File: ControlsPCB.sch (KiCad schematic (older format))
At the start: 7 parts, among them J1 8P8C_Shielded, J2 8P8C_Shielded

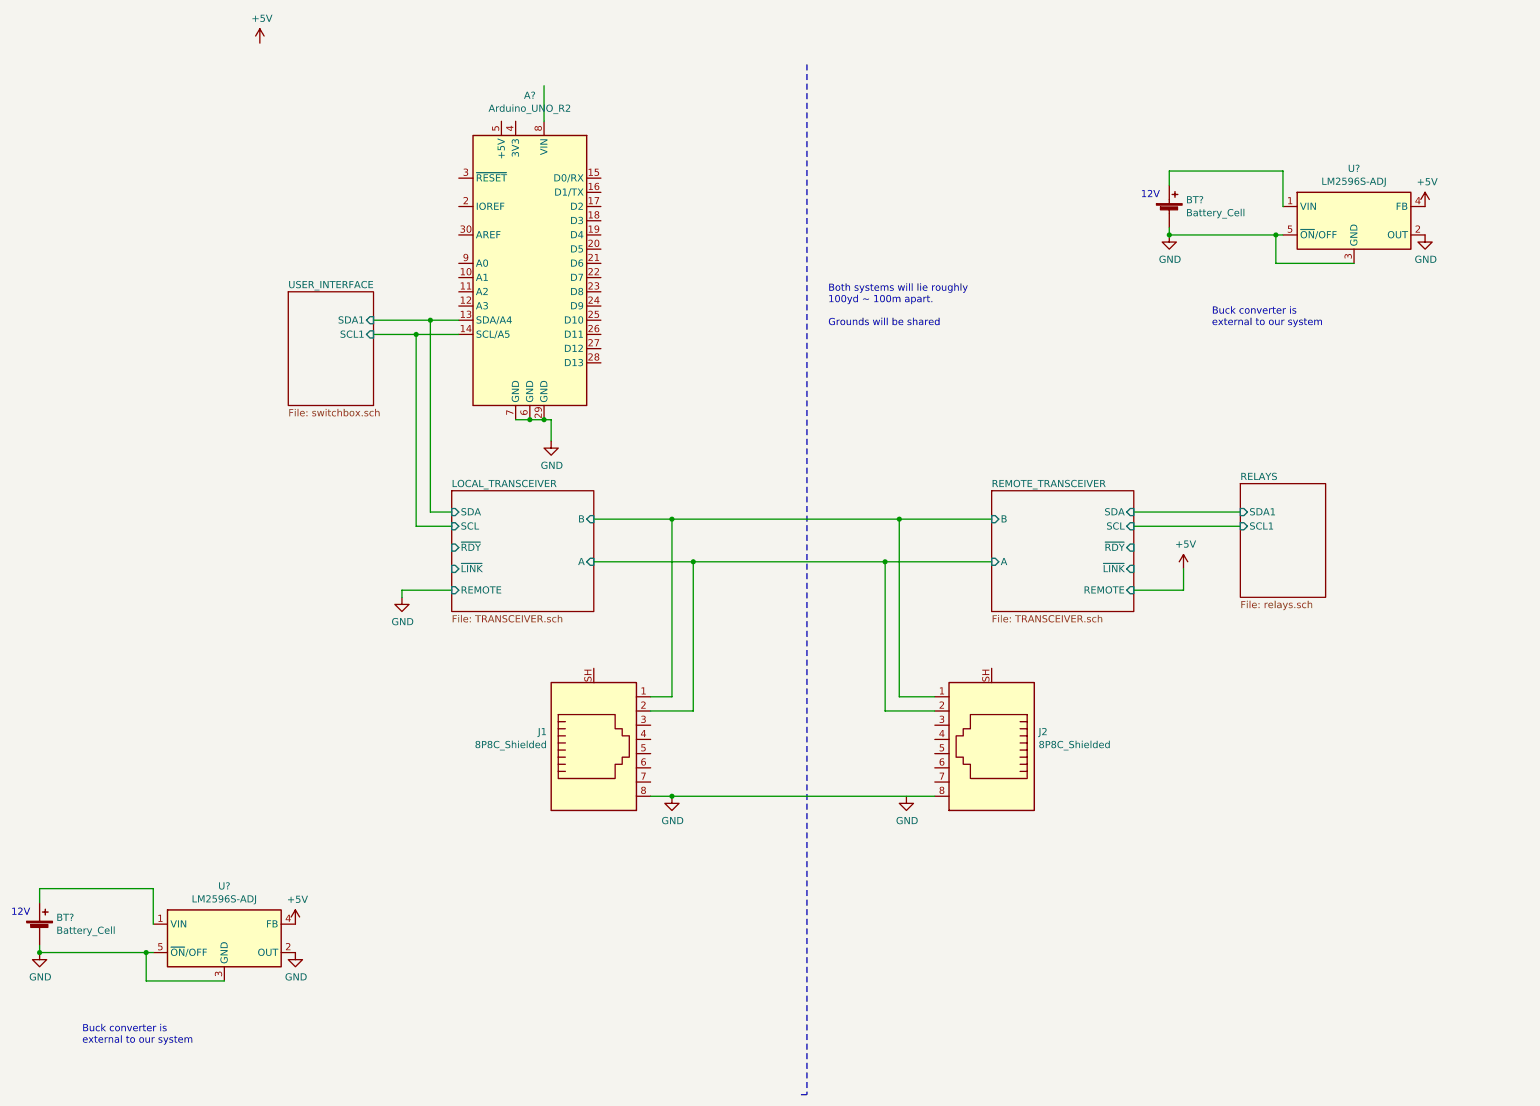
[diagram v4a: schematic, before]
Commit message: Got rid of overlying duplicate parts
Some identical parts were placed over eachother which showed up when annotating references
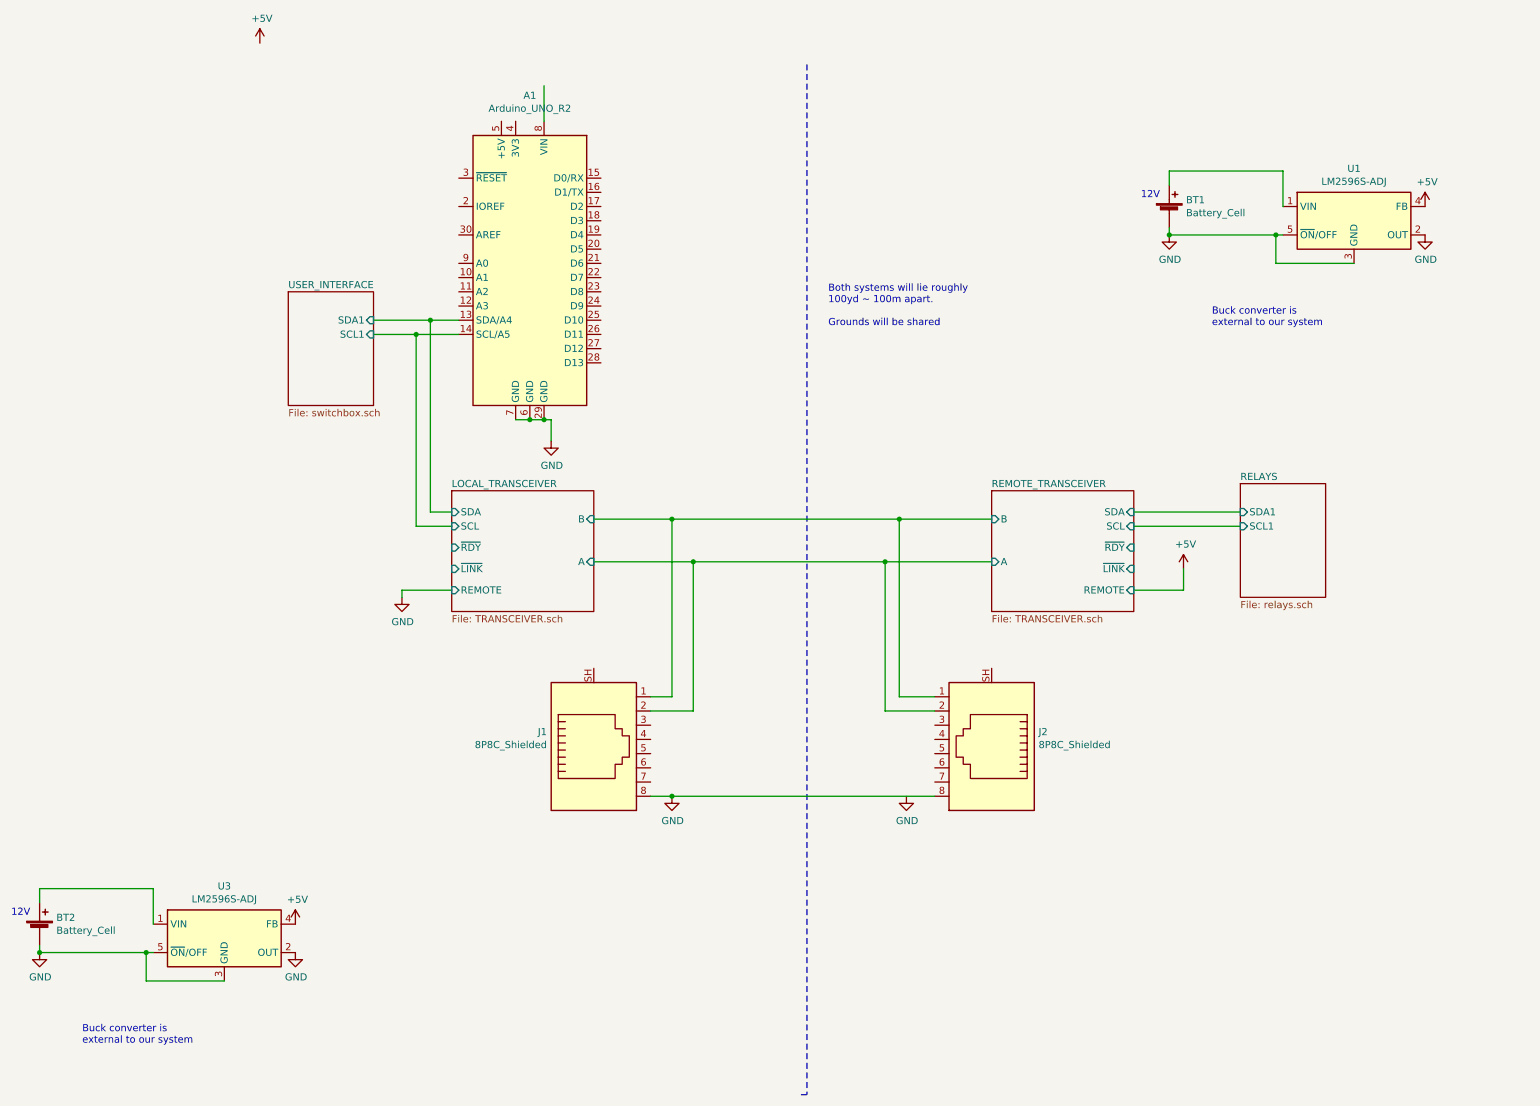
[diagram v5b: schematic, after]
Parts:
- gave numbers to parts that had none: 5
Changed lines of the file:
@@
 P 2650 6600
 AR Path="/5F57B52C/5F73A08B" Ref="#PWR?"  Part="1"
-AR Path="/5F73A08B" Ref="#PWR?"  Part="1"
-F 0 "#PWR?" H 2650 6450 50  0001 C CNN
+AR Path="/5F73A08B" Ref="#PWR0114"  Part="1"
+F 0 "#PWR0114" H 2650 6450 50  0001 C CNN
 F 1 "+5V" H 2665 6773 50  0000 C CNN
 F 2 "" H 2650 6600 50  0001 C CNN
@@
 P 2650 6800
 AR Path="/5F57B52C/5F73A091" Ref="#PWR?"  Part="1"
-AR Path="/5F73A091" Ref="#PWR?"  Part="1"
-F 0 "#PWR?" H 2650 6550 50  0001 C CNN
+AR Path="/5F73A091" Ref="#PWR0115"  Part="1"
+F 0 "#PWR0115" H 2650 6550 50  0001 C CNN
 F 1 "GND" H 2655 6627 50  0000 C CNN
 F 2 "" H 2650 6800 50  0001 C CNN
@@
 P 2150 6700
 AR Path="/5F57B52C/5F73A0A3" Ref="U?"  Part="1"
-AR Path="/5F73A0A3" Ref="U?"  Part="1"
-F 0 "U?" H 2150 7067 50  0000 C CNN
+AR Path="/5F73A0A3" Ref="U3"  Part="1"
+F 0 "U3" H 2150 7067 50  0000 C CNN
 F 1 "LM2596S-ADJ" H 2150 6976 50  0000 C CNN
 F 2 "Package_TO_SOT_SMD:TO-263-5_TabPin3" H 2200 6450 50  0001 L CIN
@@
 P 850 6650
 AR Path="/5F57B52C/5F73A0A9" Ref="BT?"  Part="1"
-AR Path="/5F73A0A9" Ref="BT?"  Part="1"
-F 0 "BT?" H 968 6746 50  0000 L CNN
+AR Path="/5F73A0A9" Ref="BT2"  Part="1"
+F 0 "BT2" H 968 6746 50  0000 L CNN
 F 1 "Battery_Cell" H 968 6655 50  0000 L CNN
 F 2 "" V 850 6710 50  0001 C CNN
@@
 P 850 6800
 AR Path="/5F57B52C/5F73EC1F" Ref="#PWR?"  Part="1"
-AR Path="/5F73EC1F" Ref="#PWR?"  Part="1"
-F 0 "#PWR?" H 850 6550 50  0001 C CNN
+AR Path="/5F73EC1F" Ref="#PWR0125"  Part="1"
+F 0 "#PWR0125" H 850 6550 50  0001 C CNN
 F 1 "GND" H 855 6627 50  0000 C CNN
 F 2 "" H 850 6800 50  0001 C CNN
@@
 Connection ~ 850  6800
 $Comp
-L MCU_Module:Arduino_UNO_R2 A?
+L MCU_Module:Arduino_UNO_R2 A1
 U 1 1 5F74B67E
 P 4300 1950
-AR Path="/5F74B67E" Ref="A?"  Part="1"
+AR Path="/5F74B67E" Ref="A1"  Part="1"
 AR Path="/5F6BFC31/5F74B67E" Ref="A?"  Part="1"
-F 0 "A?" H 4300 3131 50  0000 C CNN
+F 0 "A1" H 4300 3131 50  0000 C CNN
 F 1 "Arduino_UNO_R2" H 4300 3040 50  0000 C CNN
 F 2 "Module:Arduino_UNO_R2" H 4300 1950 50  0001 C CIN
@@
 P 2400 400
 AR Path="/5F57B52C/5F7512D5" Ref="#PWR?"  Part="1"
-AR Path="/5F7512D5" Ref="#PWR?"  Part="1"
-F 0 "#PWR?" H 2400 250 50  0001 C CNN
+AR Path="/5F7512D5" Ref="#PWR0126"  Part="1"
+F 0 "#PWR0126" H 2400 250 50  0001 C CNN
 F 1 "+5V" H 2415 573 50  0000 C CNN
 F 2 "" H 2400 400 50  0001 C CNN
@@
 	4400 3050 4450 3050
 $Comp
-L power:GND #PWR?
+L power:GND #PWR0127
 U 1 1 5F753983
 P 4450 3200
-F 0 "#PWR?" H 4450 2950 50  0001 C CNN
+F 0 "#PWR0127" H 4450 2950 50  0001 C CNN
 F 1 "GND" H 4455 3027 50  0000 C CNN
 F 2 "" H 4450 3200 50  0001 C CNN
@@
 	3500 2450 3800 2450
 $Comp
-L power:GND #PWR?
+L power:GND #PWR0128
 U 1 1 5F78DE7A
 P 3400 4300
-F 0 "#PWR?" H 3400 4050 50  0001 C CNN
+F 0 "#PWR0128" H 3400 4050 50  0001 C CNN
 F 1 "GND" H 3405 4127 50  0000 C CNN
 F 2 "" H 3400 4300 50  0001 C CNN
@@
 	3400 4250 3750 4250
 $Comp
-L power:+5V #PWR?
+L power:+5V #PWR0129
 U 1 1 5F7956F2
 P 8900 4100
-F 0 "#PWR?" H 8900 3950 50  0001 C CNN
+F 0 "#PWR0129" H 8900 3950 50  0001 C CNN
 F 1 "+5V" H 8915 4273 50  0000 C CNN
 F 2 "" H 8900 4100 50  0001 C CNN
@@
 P 10600 1550
 AR Path="/5F57B52C/5F7F4E76" Ref="#PWR?"  Part="1"
-AR Path="/5F7F4E76" Ref="#PWR?"  Part="1"
-F 0 "#PWR?" H 10600 1400 50  0001 C CNN
+AR Path="/5F7F4E76" Ref="#PWR0130"  Part="1"
+F 0 "#PWR0130" H 10600 1400 50  0001 C CNN
 F 1 "+5V" H 10615 1723 50  0000 C CNN
 F 2 "" H 10600 1550 50  0001 C CNN
@@
 P 10600 1750
 AR Path="/5F57B52C/5F7F4E7C" Ref="#PWR?"  Part="1"
-AR Path="/5F7F4E7C" Ref="#PWR?"  Part="1"
-F 0 "#PWR?" H 10600 1500 50  0001 C CNN
+AR Path="/5F7F4E7C" Ref="#PWR0131"  Part="1"
+F 0 "#PWR0131" H 10600 1500 50  0001 C CNN
 F 1 "GND" H 10605 1577 50  0000 C CNN
 F 2 "" H 10600 1750 50  0001 C CNN
@@
 P 10100 1650
 AR Path="/5F57B52C/5F7F4E83" Ref="U?"  Part="1"
-AR Path="/5F7F4E83" Ref="U?"  Part="1"
-F 0 "U?" H 10100 2017 50  0000 C CNN
+AR Path="/5F7F4E83" Ref="U1"  Part="1"
+F 0 "U1" H 10100 2017 50  0000 C CNN
 F 1 "LM2596S-ADJ" H 10100 1926 50  0000 C CNN
 F 2 "Package_TO_SOT_SMD:TO-263-5_TabPin3" H 10150 1400 50  0001 L CIN
@@
 P 8800 1600
 AR Path="/5F57B52C/5F7F4E89" Ref="BT?"  Part="1"
-AR Path="/5F7F4E89" Ref="BT?"  Part="1"
-F 0 "BT?" H 8918 1696 50  0000 L CNN
+AR Path="/5F7F4E89" Ref="BT1"  Part="1"
+F 0 "BT1" H 8918 1696 50  0000 L CNN
 F 1 "Battery_Cell" H 8918 1605 50  0000 L CNN
 F 2 "" V 8800 1660 50  0001 C CNN
@@
 P 8800 1750
 AR Path="/5F57B52C/5F7F4E99" Ref="#PWR?"  Part="1"
-AR Path="/5F7F4E99" Ref="#PWR?"  Part="1"
-F 0 "#PWR?" H 8800 1500 50  0001 C CNN
+AR Path="/5F7F4E99" Ref="#PWR0132"  Part="1"
+F 0 "#PWR0132" H 8800 1500 50  0001 C CNN
 F 1 "GND" H 8805 1577 50  0000 C CNN
 F 2 "" H 8800 1750 50  0001 C CNN
@@
 	5150 5700 5300 5700
 $Comp
-L power:GND #PWR?
+L power:GND #PWR0133
 U 1 1 5F7F7C99
 P 5300 5700
-F 0 "#PWR?" H 5300 5450 50  0001 C CNN
+F 0 "#PWR0133" H 5300 5450 50  0001 C CNN
 F 1 "GND" H 5305 5527 50  0000 C CNN
 F 2 "" H 5300 5700 50  0001 C CNN
@@
 	5300 5700 7150 5700
 $Comp
-L power:GND #PWR?
+L power:GND #PWR0134
 U 1 1 5F7F9662
 P 6950 5700
-F 0 "#PWR?" H 6950 5450 50  0001 C CNN
+F 0 "#PWR0134" H 6950 5450 50  0001 C CNN
 F 1 "GND" H 6955 5527 50  0000 C CNN
 F 2 "" H 6950 5700 50  0001 C CNN
